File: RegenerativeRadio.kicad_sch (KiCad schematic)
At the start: 36 parts, among them P1 500kΩ (log)

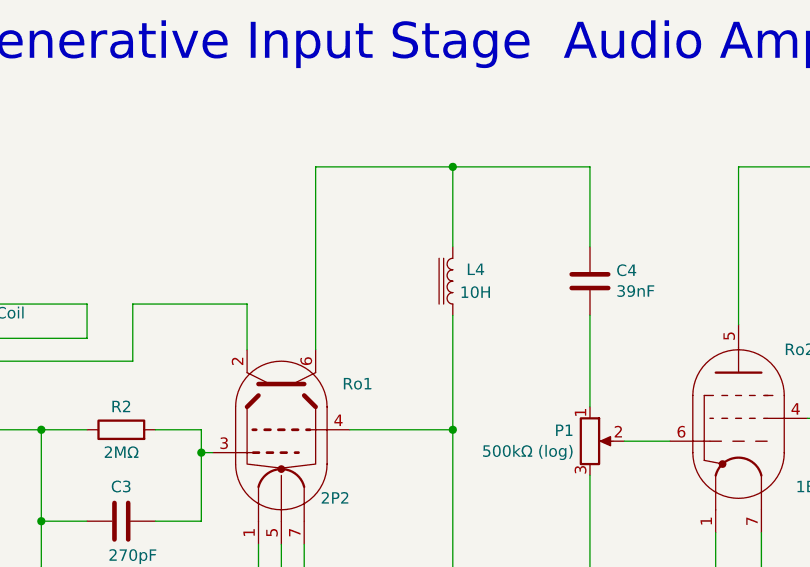
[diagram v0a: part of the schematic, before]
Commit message: Update documentation, add LM317 simultion
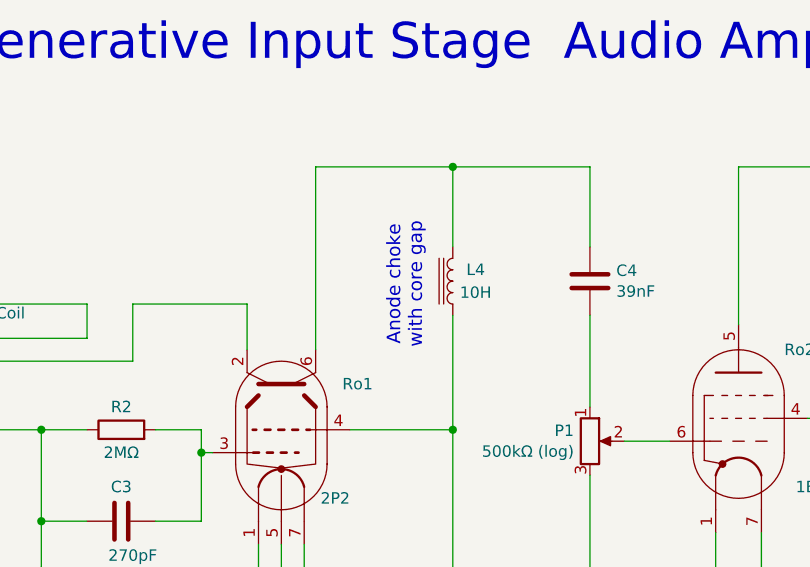
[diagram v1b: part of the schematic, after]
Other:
- note added: "Anode choke with core gap"
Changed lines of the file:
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@@
+		)
+	)
+	(text "Anode choke\nwith core gap"
+		(exclude_from_sim no)
+		(at 89.916 77.978 90)
+		(effects
+			(font
+				(size 1.5 1.5)
+			)
 		)
 	)

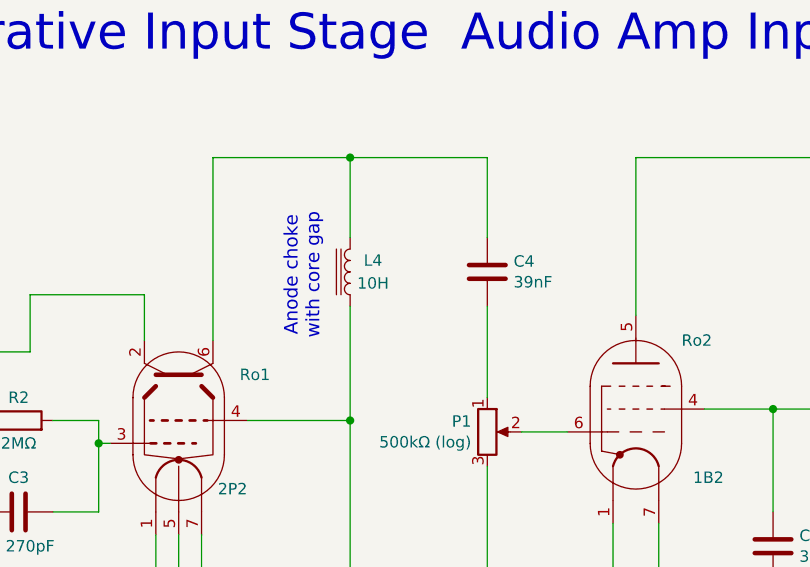
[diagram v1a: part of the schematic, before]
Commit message: Update RegenerativeRadio.kicad_sch
Change value of anode choke L4. Inductance range is 6H to 10H.
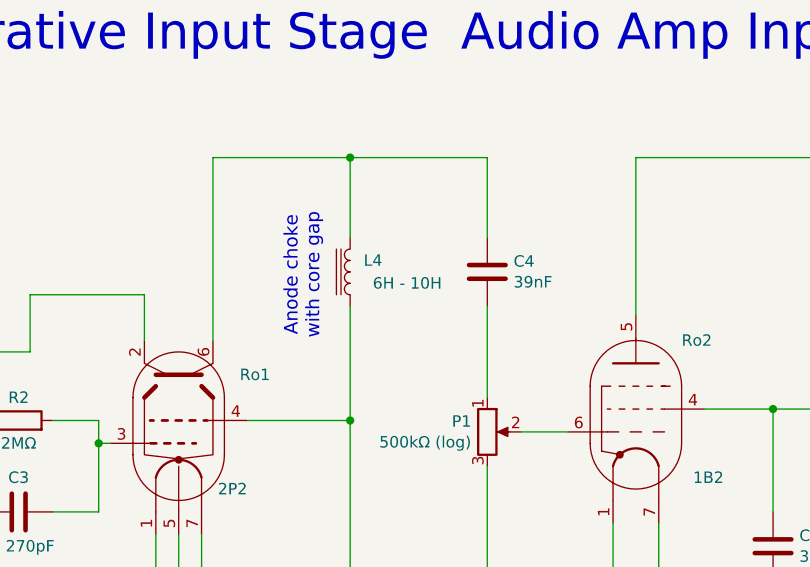
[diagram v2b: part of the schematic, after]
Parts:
- L4: value 10H -> 6H - 10H
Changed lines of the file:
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@@
 			)
 		)
-		(property "Value" "10H"
-			(at 97.79 78.74 0)
+		(property "Value" "6H - 10H"
+			(at 101.6 78.74 0)
 			(effects
 				(font
